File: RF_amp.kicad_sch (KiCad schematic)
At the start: 21 parts, among them T1 FT50-74 (22:4), U1 LT1253, U2 QPR_Filter

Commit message: Add AF Stage
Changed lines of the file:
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@@
-    (pin "1")
-  )
-  (symbol (lib_id "power:PWR_FLAG") (at 190.5 68.58 0) (unit 1)
-    (in_bom yes) (on_board yes) (fields_autoplaced)
-    (property "Reference" "#FLG02" (id 0) (at 190.5 66.675 0)
-      (effects (font (size 1.27 1.27)) hide)
-    )
-    (property "Value" "PWR_FLAG" (id 1) (at 193.04 67.3099 0)
-      (effects (font (size 1.27 1.27)) (justify left))
-    )
-    (property "Footprint" "" (id 2) (at 190.5 68.58 0)
-      (effects (font (size 1.27 1.27)) hide)
-    )
-    (property "Datasheet" "~" (id 3) (at 190.5 68.58 0)
-      (effects (font (size 1.27 1.27)) hide)
-    )
     (pin "1")
   )
@@
     (pin "4")
   )
-  (symbol (lib_id "power:GND") (at 190.5 68.58 0) (unit 1)
-    (in_bom yes) (on_board yes) (fields_autoplaced)
-    (property "Reference" "#PWR010" (id 0) (at 190.5 74.93 0)
-      (effects (font (size 1.27 1.27)) hide)
-    )
-    (property "Value" "GND" (id 1) (at 190.5 73.66 0))
-    (property "Footprint" "" (id 2) (at 190.5 68.58 0)
-      (effects (font (size 1.27 1.27)) hide)
-    )
-    (property "Datasheet" "" (id 3) (at 190.5 68.58 0)
-      (effects (font (size 1.27 1.27)) hide)
-    )
-    (pin "1")
-  )
   (symbol (lib_id "Custom_RF:LT1253") (at 88.9 101.6 0) (unit 1)

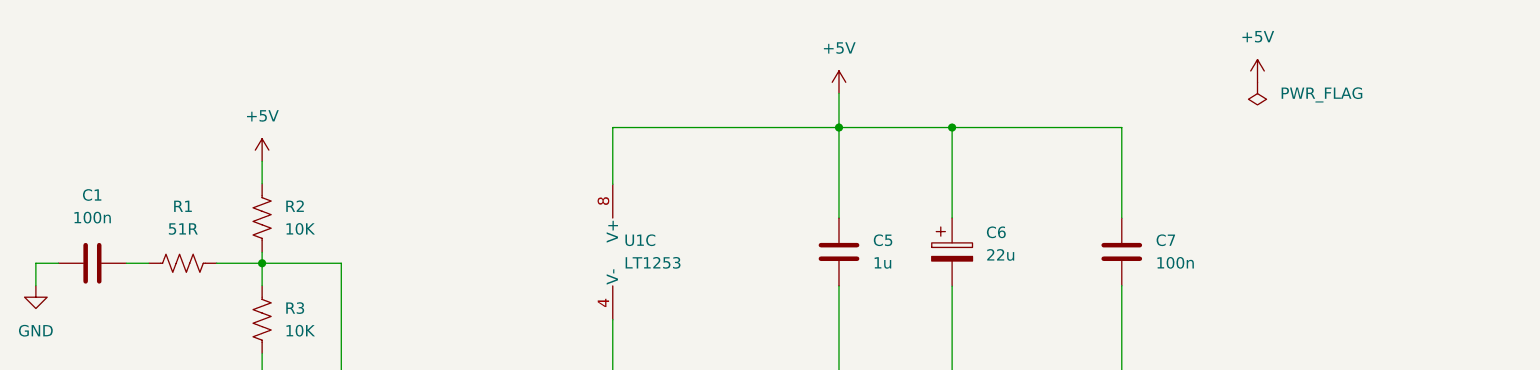
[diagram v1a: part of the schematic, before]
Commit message: Continue Migration from D612
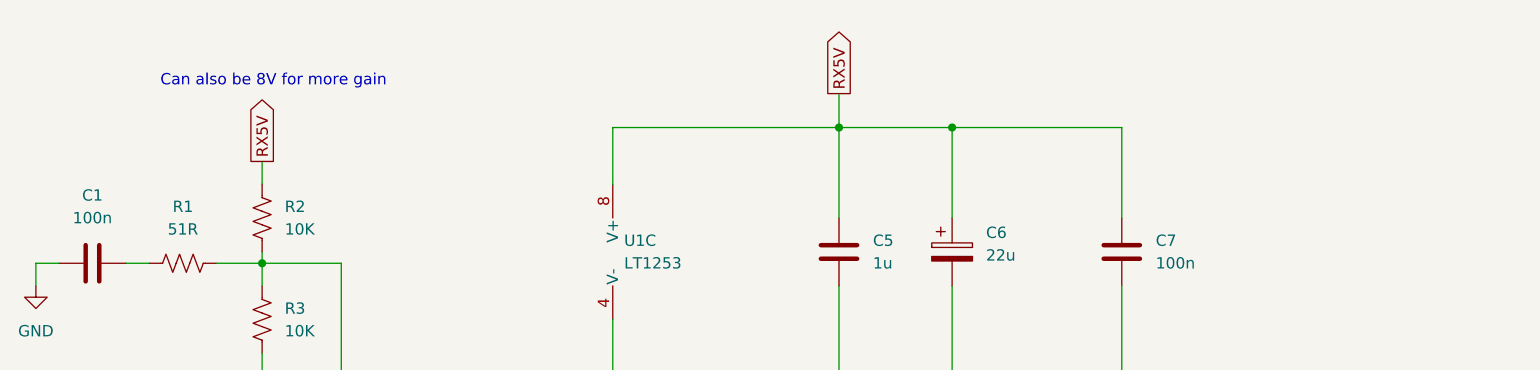
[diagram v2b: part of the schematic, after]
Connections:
- net +5V renamed RX5V
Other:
- note added: "Can also be 8V for more gain"
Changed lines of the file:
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@@
     (stroke (width 0) (type default) (color 0 0 0 0))
+  )
+  (text "Can also be 8V for more gain" (at 67.31 47.625 0)
+    (effects (font (size 1.27 1.27)) (justify left bottom))
   )
   (global_label "IFRFIN" (shape input) (at 241.3 110.49 0) (fields_autoplaced)
@@
     )
   )
+  (global_label "RX5V" (shape output) (at 78.74 55.88 90) (fields_autoplaced)
+    (effects (font (size 1.27 1.27)) (justify left))
+    (property "Intersheet References" "${INTERSHEET_REFS}" (id 0) (at 78.6606 48.6893 90)
+      (effects (font (size 1.27 1.27)) (justify left) hide)
+    )
+  )
+  (global_label "RX5V" (shape output) (at 143.51 48.26 90) (fields_autoplaced)
+    (effects (font (size 1.27 1.27)) (justify left))
+    (property "Intersheet References" "${INTERSHEET_REFS}" (id 0) (at 143.4306 41.0693 90)
+      (effects (font (size 1.27 1.27)) (justify left) hide)
+    )
+  )
   (symbol (lib_id "Device:C") (at 143.51 66.04 0) (unit 1)
     (in_bom yes) (on_board yes) (fields_autoplaced)
@@
   (symbol (lib_id "power:GND") (at 165.1 120.65 0) (unit 1)
     (in_bom yes) (on_board yes) (fields_autoplaced)
-    (property "Reference" "#PWR08" (id 0) (at 165.1 127 0)
+    (property "Reference" "#PWR06" (id 0) (at 165.1 127 0)
       (effects (font (size 1.27 1.27)) hide)
     )
@@
   (symbol (lib_id "power:GND") (at 218.44 125.73 0) (unit 1)
     (in_bom yes) (on_board yes) (fields_autoplaced)
-    (property "Reference" "#PWR011" (id 0) (at 218.44 132.08 0)
+    (property "Reference" "#PWR07" (id 0) (at 218.44 132.08 0)
       (effects (font (size 1.27 1.27)) hide)
     )
@@
   (symbol (lib_id "power:GND") (at 128.27 148.59 0) (unit 1)
     (in_bom yes) (on_board yes) (fields_autoplaced)
-    (property "Reference" "#PWR05" (id 0) (at 128.27 154.94 0)
+    (property "Reference" "#PWR04" (id 0) (at 128.27 154.94 0)
       (effects (font (size 1.27 1.27)) hide)
     )
@@
   (symbol (lib_id "power:GND") (at 81.28 148.59 0) (unit 1)
     (in_bom yes) (on_board yes) (fields_autoplaced)
-    (property "Reference" "#PWR04" (id 0) (at 81.28 154.94 0)
+    (property "Reference" "#PWR03" (id 0) (at 81.28 154.94 0)
       (effects (font (size 1.27 1.27)) hide)
     )
@@
     (pin "2")
   )
-  (symbol (lib_id "power:+5V") (at 78.74 55.88 0) (unit 1)
-    (in_bom yes) (on_board yes) (fields_autoplaced)
-    (property "Reference" "#PWR02" (id 0) (at 78.74 59.69 0)
-      (effects (font (size 1.27 1.27)) hide)
-    )
-    (property "Value" "+5V" (id 1) (at 78.74 50.8 0))
-    (property "Footprint" "" (id 2) (at 78.74 55.88 0)
-      (effects (font (size 1.27 1.27)) hide)
-    )
-    (property "Datasheet" "" (id 3) (at 78.74 55.88 0)
-      (effects (font (size 1.27 1.27)) hide)
-    )
-    (pin "1")
-  )
   (symbol (lib_id "Device:R_Potentiometer_Trim") (at 128.27 125.73 0) (unit 1)
     (in_bom yes) (on_board yes) (fields_autoplaced)
@@
     (pin "3")
   )
-  (symbol (lib_id "power:+5V") (at 143.51 48.26 0) (unit 1)
-    (in_bom yes) (on_board yes) (fields_autoplaced)
-    (property "Reference" "#PWR06" (id 0) (at 143.51 52.07 0)
-      (effects (font (size 1.27 1.27)) hide)
-    )
-    (property "Value" "+5V" (id 1) (at 143.51 43.18 0))
-    (property "Footprint" "" (id 2) (at 143.51 48.26 0)
-      (effects (font (size 1.27 1.27)) hide)
-    )
-    (property "Datasheet" "" (id 3) (at 143.51 48.26 0)
-      (effects (font (size 1.27 1.27)) hide)
-    )
-    (pin "1")
-  )
   (symbol (lib_id "Device:R_US") (at 78.74 73.66 0) (unit 1)
     (in_bom yes) (on_board yes) (fields_autoplaced)
@@
   (symbol (lib_id "power:GND") (at 78.74 80.01 0) (unit 1)
     (in_bom yes) (on_board yes) (fields_autoplaced)
-    (property "Reference" "#PWR03" (id 0) (at 78.74 86.36 0)
+    (property "Reference" "#PWR02" (id 0) (at 78.74 86.36 0)
       (effects (font (size 1.27 1.27)) hide)
     )
@@
     (pin "1")
   )
-  (symbol (lib_id "power:PWR_FLAG") (at 190.5 46.99 180) (unit 1)
-    (in_bom yes) (on_board yes) (fields_autoplaced)
-    (property "Reference" "#FLG01" (id 0) (at 190.5 48.895 0)
-      (effects (font (size 1.27 1.27)) hide)
-    )
-    (property "Value" "PWR_FLAG" (id 1) (at 193.04 48.2599 0)
-      (effects (font (size 1.27 1.27)) (justify right))
-    )
-    (property "Footprint" "" (id 2) (at 190.5 46.99 0)
-      (effects (font (size 1.27 1.27)) hide)
-    )
-    (property "Datasheet" "~" (id 3) (at 190.5 46.99 0)
-      (effects (font (size 1.27 1.27)) hide)
-    )
-    (pin "1")
-  )
   (symbol (lib_id "power:GND") (at 143.51 83.82 0) (unit 1)
     (in_bom yes) (on_board yes) (fields_autoplaced)
-    (property "Reference" "#PWR07" (id 0) (at 143.51 90.17 0)
+    (property "Reference" "#PWR05" (id 0) (at 143.51 90.17 0)
       (effects (font (size 1.27 1.27)) hide)
     )
@@
     (pin "2")
   )
-  (symbol (lib_id "power:+5V") (at 190.5 46.99 0) (unit 1)
-    (in_bom yes) (on_board yes) (fields_autoplaced)
-    (property "Reference" "#PWR09" (id 0) (at 190.5 50.8 0)
-      (effects (font (size 1.27 1.27)) hide)
-    )
-    (property "Value" "+5V" (id 1) (at 190.5 41.91 0))
-    (property "Footprint" "" (id 2) (at 190.5 46.99 0)
-      (effects (font (size 1.27 1.27)) hide)
-    )
-    (property "Datasheet" "" (id 3) (at 190.5 46.99 0)
-      (effects (font (size 1.27 1.27)) hide)
-    )
-    (pin "1")
-  )
   (symbol (lib_id "Device:Transformer_1P_1S") (at 179.07 111.76 0) (unit 1)

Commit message: Update
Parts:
- removed R1: 51R, Resistor_THT:R_Axial_DIN0207_L6.3mm_D2.5mm_P10.16mm_Horizontal, symbol Device:R_US
- added C4: 100n, Capacitor_THT:C_Disc_D3.4mm_W2.1mm_P2.50mm, symbol Device:C
- added J1: ANT_IN, Connector_Coaxial:SMA_Amphenol_901-144_Vertical, symbol Connector:Conn_Coaxial
- added R4: 51R, Resistor_THT:R_Axial_DIN0207_L6.3mm_D2.5mm_P10.16mm_Horizontal, symbol Device:R_US
- C1: value 100n -> 1u
- renumbered C4 to C5, C5 to C6, C6 to C7, C7 to C8, R2 to R1, R3 to R2, R4 to R3
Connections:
- net GND: now also C4.2, J1.2 (Ext)
- net at C1.1: now also R1.2, R2.1, C4.1, R4.2
- net at C2.2, U1.3 (InA+): now also R4.1; no longer R1.2, R2.1
- net ANT_IN: no longer names the net of C2.1
- net ANT_IN: now also J1.1 (In)
